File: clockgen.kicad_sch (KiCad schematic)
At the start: 150 parts, among them IC3 TLV74325PDBVR, J13 73391-0083, J14 73391-0083, J15 292161-3, J16 U.FL-R-SMT-180, Q10 BSS138, Q9 BSS138, U12 AZ1117-3.3, U13 AZ1117-3.3, U14 TCA6416APWR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

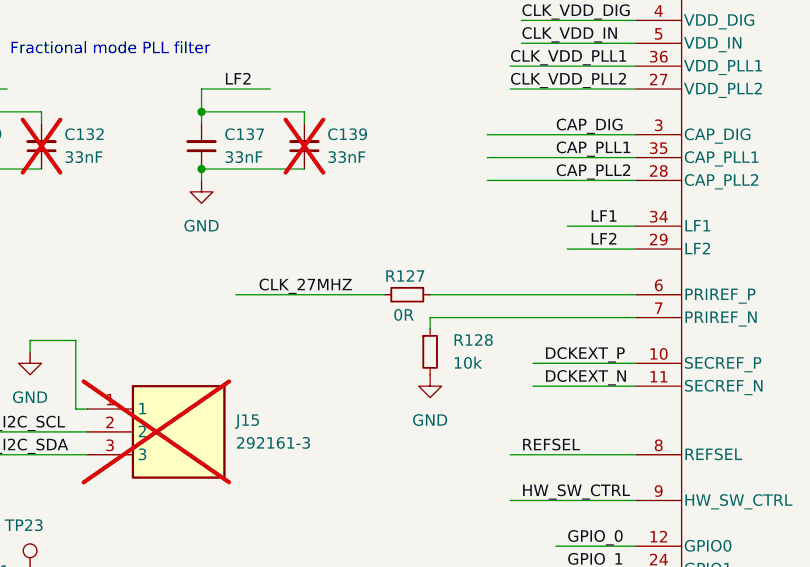
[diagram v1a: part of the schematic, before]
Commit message: schema: AC term of SOC primary clock
AC term of primary 33.333 clock
ERRATA updates
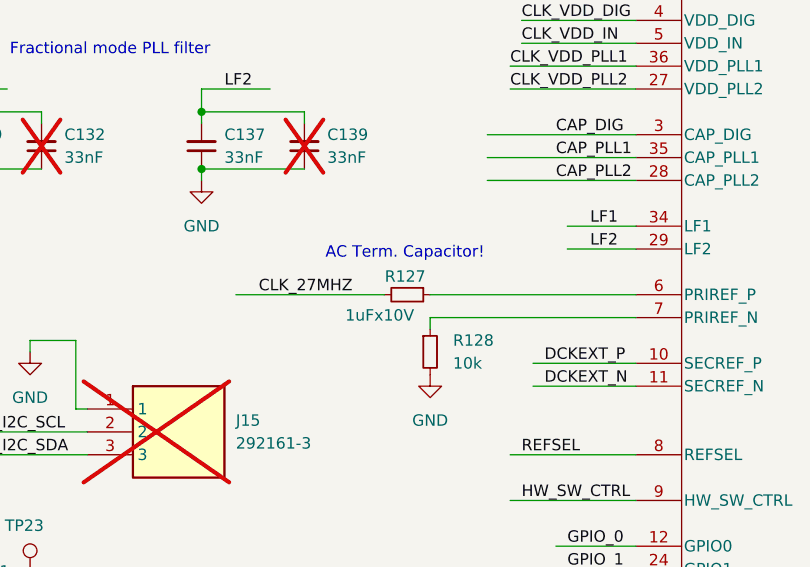
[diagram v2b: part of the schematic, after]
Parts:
- R127: value 0R -> 1uFx10V; JLCPCB Part # C2906974 -> C841050; Part FRC0603F0000TS -> (none)
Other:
- note added: "AC Term. Capacitor!"
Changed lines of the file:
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@@
 		)
 	)
+	(text "AC Term. Capacitor!"
+		(exclude_from_sim no)
+		(at 263.906 116.078 0)
+		(effects
+			(font
+				(size 1.27 1.27)
+			)
+		)
+	)
 	(text "DCK2 -> clock to external device"
 		(exclude_from_sim no)
@@
 			)
 		)
-		(property "Value" "0R"
+		(property "Value" "1uFx10V"
 			(at 264.922 122.936 90)
 			(effects
@@
 			)
 		)
-		(property "JLCPCB Part #" "C2906974"
+		(property "JLCPCB Part #" "C841050"
 			(at 264.16 120.65 0)
 			(effects
@@
 			)
 		)
-		(property "Part" "FRC0603F0000TS"
+		(property "Part" ""
 			(at 264.16 120.65 90)
 			(effects

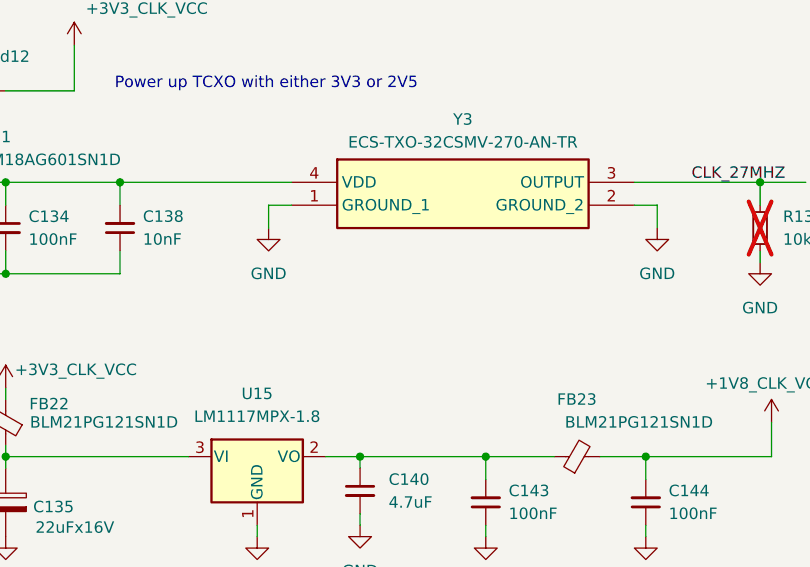
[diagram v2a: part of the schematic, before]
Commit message: P2C SYZYGY clock lines polarity fix, allow Y3 TCXO with pin1 ENA
Swapped polarity on SYZYGY P2C clock lines were fixed
Two additional resistors R71 & R64 were introduced to allow a TCXO with ENA input
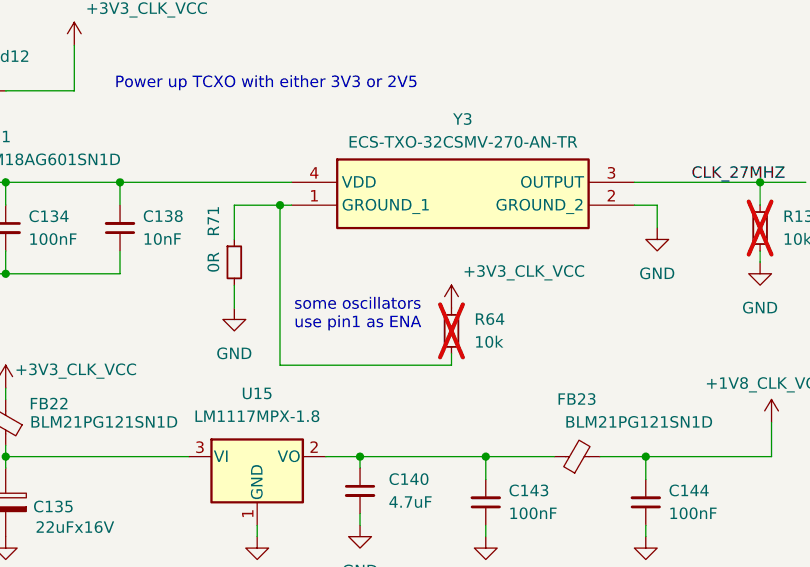
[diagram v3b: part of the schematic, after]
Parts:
- added R64: 10k, Resistor_SMD:R_0402_1005Metric, symbol Device:R_Small
- added R71: 0R, Resistor_SMD:R_0402_1005Metric, symbol Device:R_Small
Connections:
- net +3V3_CLK_VCC: now also R64.1
- net GND: now also R71.2; no longer Y3.1 (GROUND_1)
- new net: R64.2, R71.1, Y3.1 (GROUND_1)
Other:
- note added: "some oscillators use pin1 as ENA"
